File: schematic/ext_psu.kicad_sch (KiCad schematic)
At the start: 0 parts

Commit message: RF modulator completed, rough draft complete. Next step is to clean-up all pages.
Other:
- note added: "MEAN WELL 28.5 Watt PSU: GP25A13D-R1B GP25B13A-R1B"
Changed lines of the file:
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@@
 (kicad_sch (version 20211123) (generator eeschema)
   (paper "A4")
+  (text "MEAN WELL 28.5 Watt PSU:\n\nGP25A13D-R1B\n\nGP25B13A-R1B\n\n"
+    (at 135.89 93.345 0)
+    (effects (font (size 1.27 1.27)) (justify left bottom))
+  )
 )

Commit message: adjusted size of the sheets. added pcb version to the rev field. F.0... the 0 is for future fixes on my end. RF PCB is E.0.
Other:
- title: (none) -> Colecovision Schematic
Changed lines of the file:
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@@
 (kicad_sch (version 20211123) (generator eeschema)
-  (paper "A4")
+  (paper "USLetter")
+  (title_block
+    (title "Colecovision Schematic")
+    (date "2023-01-09")
+    (rev "F.0")
+    (comment 1 "Jay Convertino")
+  )
   (text "MEAN WELL 28.5 Watt PSU:\n\nGP25A13D-R1B\n\nGP25B13A-R1B\n\n"
     (at 135.89 93.345 0)

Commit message: updated schematic with new layout
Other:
- company: (none) -> sparkletron
- title: Colecovision Schematic -> Reverse Engineer Colecovision
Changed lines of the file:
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@@
   (paper "USLetter")
   (title_block
-    (title "Colecovision Schematic")
-    (date "2023-01-09")
-    (rev "F.0")
+    (title "Reverse Engineer Colecovision")
+    (date "2023-03-14")
+    (rev "DEV")
+    (company "sparkletron")
     (comment 1 "Jay Convertino")
+    (comment 2 "MIT LICENSE")
   )
   (text "MEAN WELL 28.5 Watt PSU:\n\nGP25A13D-R1B\n\nGP25B13A-R1B\n\n"

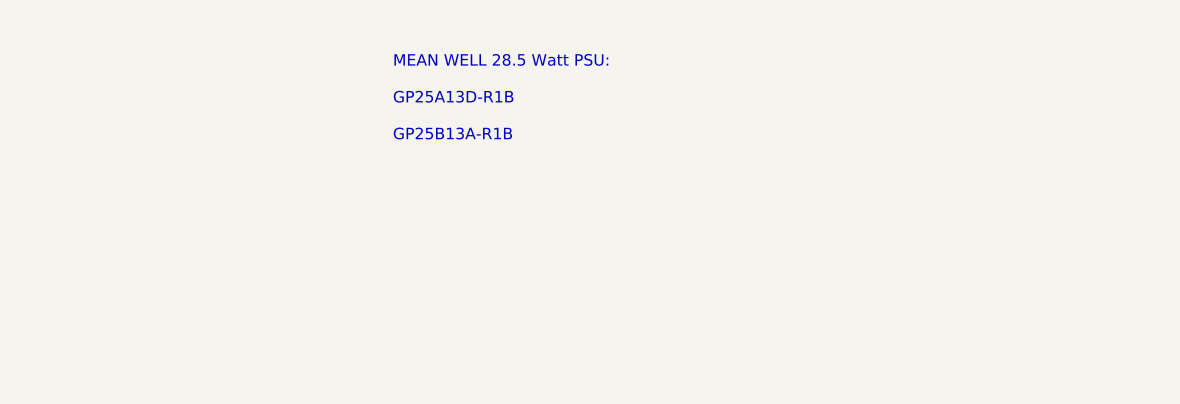
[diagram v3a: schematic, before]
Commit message: added power cable pinout, cleanup finished on main page of schematic, now fits US letter page.
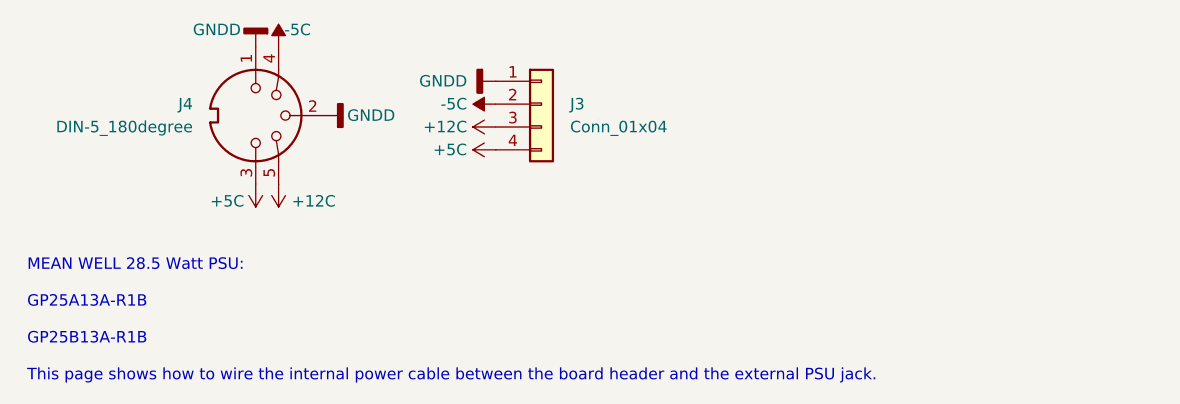
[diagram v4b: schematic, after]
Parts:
- added J3: Conn_01x04, Connector_Molex:Molex_KK-396_A-41791-0004_1x04_P3.96mm_Vertical, symbol Connector_Generic:Conn_01x04
- added J4: DIN-5_180degree, symbol Connector:DIN-5_180degree
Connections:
- new net +12C: J3.3 (Pin_3), J4.5
- new net +5C: J3.4 (Pin_4), J4.3
- new net -5C: J3.2 (Pin_2), J4.4
- new net GNDD: J3.1 (Pin_1), J4.1, J4.2
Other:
- note added: "MEAN WELL 28.5 Watt PSU: GP25A13A-R1B GP25B13A-R1B This page shows how to wire the internal power cable between the board header and the external PSU jack."
- note removed: "MEAN WELL 28.5 Watt PSU: GP25A13D-R1B GP25B13A-R1B"
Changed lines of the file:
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@@
     (comment 2 "MIT LICENSE")
   )
-  (text "MEAN WELL 28.5 Watt PSU:\n\nGP25A13D-R1B\n\nGP25B13A-R1B\n\n"
-    (at 135.89 93.345 0)
+  (text "MEAN WELL 28.5 Watt PSU:\n\nGP25A13A-R1B\n\nGP25B13A-R1B\n\nThis page shows how to wire the internal power cable between the board header and the external PSU jack.\n\n"
+    (at 95.25 120.015 0)
     (effects (font (size 1.27 1.27)) (justify left bottom))
   )
+  (symbol (lib_id "Power_Symbols:-5C") (at 123.19 80.645 0) (unit 1)
+    (in_bom yes) (on_board yes)
+    (property "Reference" "#PWR012" (id 0) (at 123.19 78.105 0)
+      (effects (font (size 1.27 1.27)) hide)
+    )
+    (property "Value" "-5C" (id 1) (at 123.825 78.74 0)
+      (effects (font (size 1.27 1.27)) (justify left))
+    )
+    (property "Footprint" "" (id 2) (at 123.19 80.645 0)
+      (effects (font (size 1.27 1.27)) hide)
+    )
+    (property "Datasheet" "" (id 3) (at 123.19 80.645 0)
+      (effects (font (size 1.27 1.27)) hide)
+    )
+    (pin "1")
+  )
+  (symbol (lib_id "power:+5C") (at 147.32 92.075 90) (unit 1)
+    (in_bom yes) (on_board yes)
+    (property "Reference" "#PWR09" (id 0) (at 151.13 92.075 0)
+      (effects (font (size 1.27 1.27)) hide)
+    )
+    (property "Value" "+5C" (id 1) (at 142.24 92.075 90))
+    (property "Footprint" "" (id 2) (at 147.32 92.075 0)
+      (effects (font (size 1.27 1.27)) hide)
+    )
+    (property "Datasheet" "" (id 3) (at 147.32 92.075 0)
+      (effects (font (size 1.27 1.27)) hide)
+    )
+    (pin "1")
+  )
+  (symbol (lib_id "power:+12C") (at 147.32 89.535 90) (unit 1)
+    (in_bom yes) (on_board yes)
+    (property "Reference" "#PWR08" (id 0) (at 151.13 89.535 0)
+      (effects (font (size 1.27 1.27)) hide)
+    )
+    (property "Value" "+12C" (id 1) (at 144.145 89.535 90)
+      (effects (font (size 1.27 1.27)) (justify left))
+    )
+    (property "Footprint" "" (id 2) (at 147.32 89.535 0)
+      (effects (font (size 1.27 1.27)) hide)
+    )
+    (property "Datasheet" "" (id 3) (at 147.32 89.535 0)
+      (effects (font (size 1.27 1.27)) hide)
+    )
+    (pin "1")
+  )
+  (symbol (lib_id "power:GNDD") (at 147.32 84.455 270) (unit 1)
+    (in_bom yes) (on_board yes)
+    (property "Reference" "#PWR06" (id 0) (at 140.97 84.455 0)
+      (effects (font (size 1.27 1.27)) hide)
+    )
+    (property "Value" "GNDD" (id 1) (at 144.145 84.455 90)
+      (effects (font (size 1.27 1.27)) (justify right))
+    )
+    (property "Footprint" "" (id 2) (at 147.32 84.455 0)
+      (effects (font (size 1.27 1.27)) hide)
+    )
+    (property "Datasheet" "" (id 3) (at 147.32 84.455 0)
+      (effects (font (size 1.27 1.27)) hide)
+    )
+    (pin "1")
+  )
+  (symbol (lib_id "power:GNDD") (at 128.27 88.265 90) (unit 1)
+    (in_bom yes) (on_board yes)
+    (property "Reference" "#PWR014" (id 0) (at 134.62 88.265 0)
+      (effects (font (size 1.27 1.27)) hide)
+    )
+    (property "Value" "GNDD" (id 1) (at 130.81 88.265 90)
+      (effects (font (size 1.27 1.27)) (justify right))
+    )
+    (property "Footprint" "" (id 2) (at 128.27 88.265 0)
+      (effects (font (size 1.27 1.27)) hide)
+    )
+    (property "Datasheet" "" (id 3) (at 128.27 88.265 0)
+      (effects (font (size 1.27 1.27)) hide)
+    )
+    (pin "1")
+  )
+  (symbol (lib_id "Connector_Generic:Conn_01x04") (at 152.4 86.995 0) (unit 1)
+    (in_bom yes) (on_board no) (fields_autoplaced)
+    (property "Reference" "J3" (id 0) (at 155.575 86.9949 0)
+      (effects (font (size 1.27 1.27)) (justify left))
+    )
+    (property "Value" "Conn_01x04" (id 1) (at 155.575 89.5349 0)
+      (effects (font (size 1.27 1.27)) (justify left))
+    )
+    (property "Footprint" "Connector_Molex:Molex_KK-396_A-41791-0004_1x04_P3.96mm_Vertical" (id 2) (at 152.4 86.995 0)
+      (effects (font (size 1.27 1.27)) hide)
+    )
+    (property "Datasheet" "~" (id 3) (at 152.4 86.995 0)
+      (effects (font (size 1.27 1.27)) hide)
+    )
+    (pin "1")
+    (pin "2")
+    (pin "3")
+    (pin "4")
+  )
+  (symbol (lib_id "power:+5C") (at 120.65 95.885 180) (unit 1)
+    (in_bom yes) (on_board yes)
+    (property "Reference" "#PWR011" (id 0) (at 120.65 92.075 0)
+      (effects (font (size 1.27 1.27)) hide)
+    )
+    (property "Value" "+5C" (id 1) (at 117.475 97.79 0))
+    (property "Footprint" "" (id 2) (at 120.65 95.885 0)
+      (effects (font (size 1.27 1.27)) hide)
+    )
+    (property "Datasheet" "" (id 3) (at 120.65 95.885 0)
+      (effects (font (size 1.27 1.27)) hide)
+    )
+    (pin "1")
+  )
+  (symbol (lib_id "power:GNDD") (at 120.65 80.645 180) (unit 1)
+    (in_bom yes) (on_board yes)
+    (property "Reference" "#PWR010" (id 0) (at 120.65 74.295 0)
+      (effects (font (size 1.27 1.27)) hide)
+    )
+    (property "Value" "GNDD" (id 1) (at 113.665 78.74 0)
+      (effects (font (size 1.27 1.27)) (justify right))
+    )
+    (property "Footprint" "" (id 2) (at 120.65 80.645 0)
+      (effects (font (size 1.27 1.27)) hide)
+    )
+    (property "Datasheet" "" (id 3) (at 120.65 80.645 0)
+      (effects (font (size 1.27 1.27)) hide)
+    )
+    (pin "1")
+  )
+  (symbol (lib_id "Connector:DIN-5_180degree") (at 120.65 88.265 270) (unit 1)
+    (in_bom yes) (on_board no) (fields_autoplaced)
+    (property "Reference" "J4" (id 0) (at 113.665 86.995 90)
+      (effects (font (size 1.27 1.27)) (justify right))
+    )
+    (property "Value" "DIN-5_180degree" (id 1) (at 113.665 89.535 90)
+      (effects (font (size 1.27 1.27)) (justify right))
+    )
+    (property "Footprint" "" (id 2) (at 120.65 88.265 0)
+      (effects (font (size 1.27 1.27)) hide)
+    )
+    (property "Datasheet" "http://www.mouser.com/ds/2/18/40_c091_abd_e-75918.pdf" (id 3) (at 120.65 88.265 0)
+      (effects (font (size 1.27 1.27)) hide)
+    )
+    (pin "1")
+    (pin "2")
+    (pin "3")
+    (pin "4")
+    (pin "5")
+  )
+  (symbol (lib_id "Power_Symbols:-5C") (at 147.32 86.995 90) (unit 1)
+    (in_bom yes) (on_board yes) (fields_autoplaced)
+    (property "Reference" "#PWR07" (id 0) (at 144.78 86.995 0)
+      (effects (font (size 1.27 1.27)) hide)
+    )
+    (property "Value" "-5C" (id 1) (at 144.145 86.9949 90)
+      (effects (font (size 1.27 1.27)) (justify left))
+    )
+    (property "Footprint" "" (id 2) (at 147.32 86.995 0)
+      (effects (font (size 1.27 1.27)) hide)
+    )
+    (property "Datasheet" "" (id 3) (at 147.32 86.995 0)
+      (effects (font (size 1.27 1.27)) hide)
+    )
+    (pin "1")
+  )
+  (symbol (lib_id "power:+12C") (at 123.19 95.885 180) (unit 1)
+    (in_bom yes) (on_board yes)
+    (property "Reference" "#PWR013" (id 0) (at 123.19 92.075 0)
+      (effects (font (size 1.27 1.27)) hide)
+    )
+    (property "Value" "+12C" (id 1) (at 129.54 97.79 0)
+      (effects (font (size 1.27 1.27)) (justify left))
+    )
+    (property "Footprint" "" (id 2) (at 123.19 95.885 0)
+      (effects (font (size 1.27 1.27)) hide)
+    )
+    (property "Datasheet" "" (id 3) (at 123.19 95.885 0)
+      (effects (font (size 1.27 1.27)) hide)
+    )
+    (pin "1")
+  )
 )
